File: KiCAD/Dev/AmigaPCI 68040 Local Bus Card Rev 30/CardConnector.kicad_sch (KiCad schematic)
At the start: 42 parts, among them CN100 DIN41612_03x40, CN111 SPI, J100 CPU CLOCK, U111 ICE40HX4K-TQ144, U409F2 W25X20CLSN, X100 40MHz

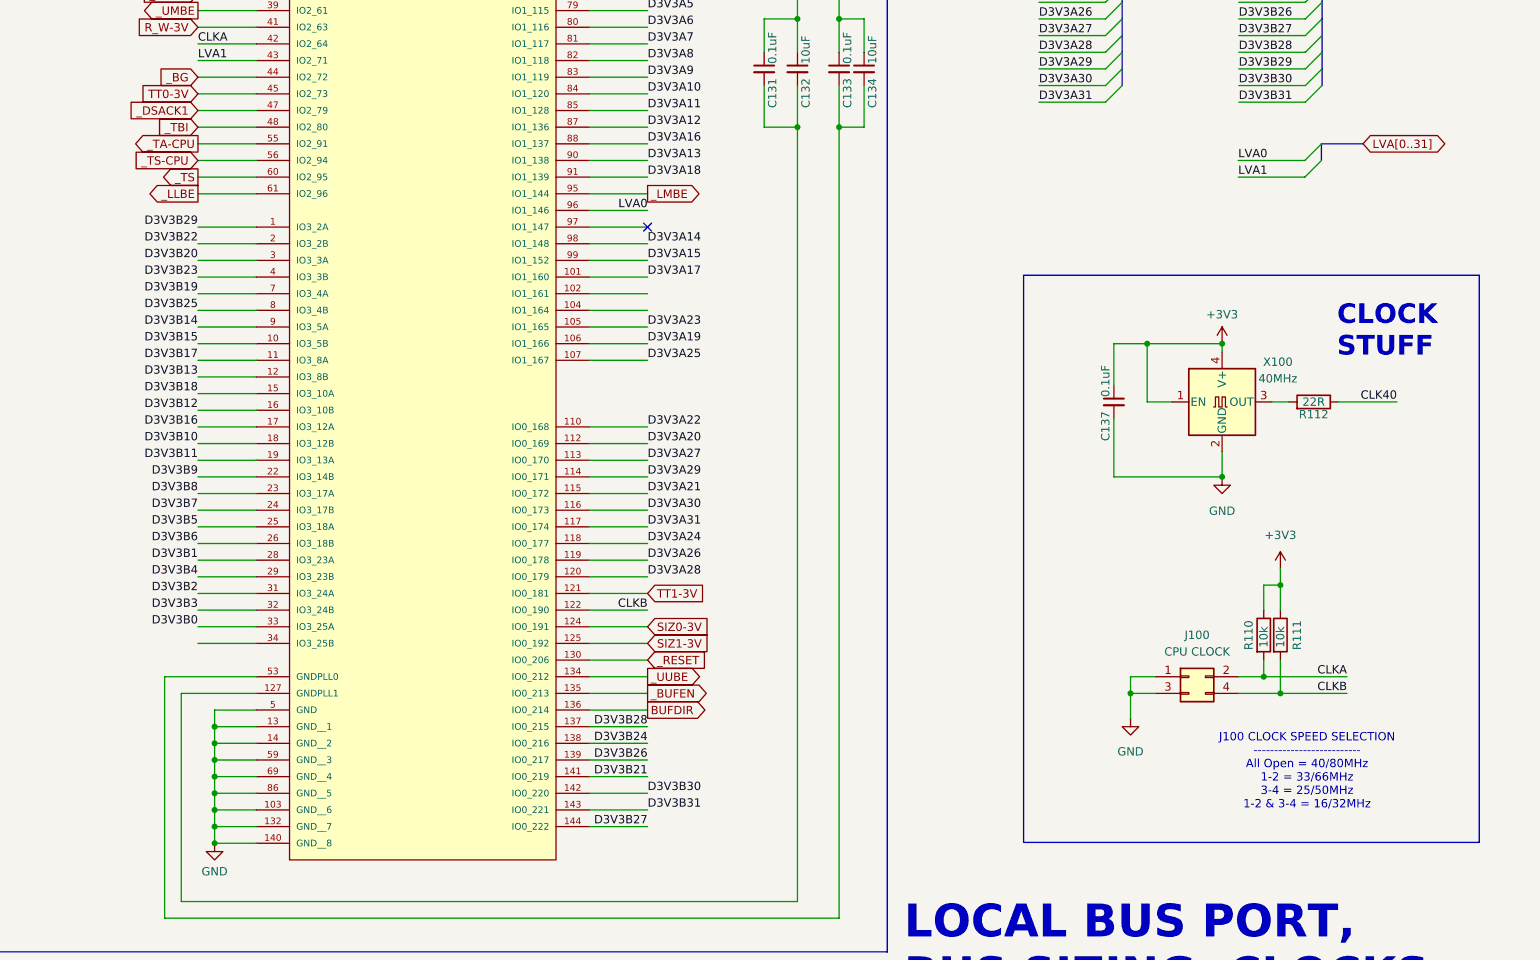
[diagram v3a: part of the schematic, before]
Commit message: CPU Local Bus Card routing. 15-JUL-2024
Board is now 6 layers to provide adequate +5V to the 68040.
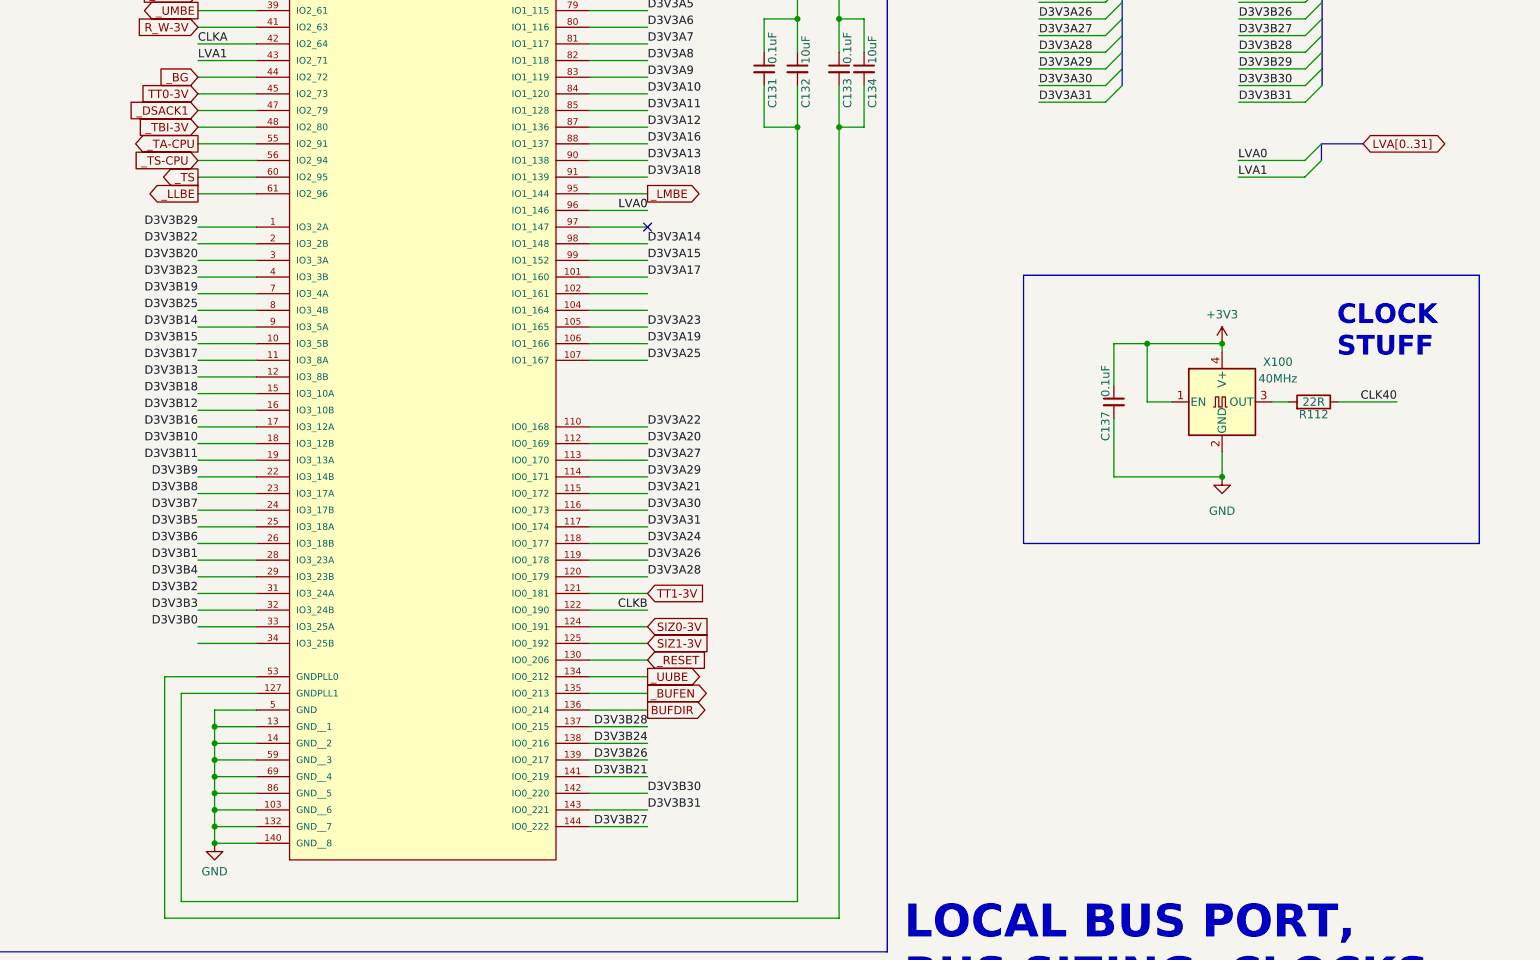
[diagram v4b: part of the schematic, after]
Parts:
- removed J100: CPU CLOCK, Connector_PinHeader_2.54mm:PinHeader_2x02_P2.54mm_Vertical, symbol Connector_Generic:Conn_02x02_Odd_Even
- removed R110, R111: 10k, Resistor_SMD:R_0603_1608Metric, symbol Device:R
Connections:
- net _TBI: no longer U111.48 (IO2_80)
- new net _TBI-3V: U111.48 (IO2_80)
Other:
- note removed: "J100 CLOCK SPEED SELECTION -------------------------- All Open = 40/80MHz 1-2 = 33/66MHz 3-4 = 25/50MHz 1-2 & 3-4 = 16/32MHz"

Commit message: CPU Local Bus Card Rev 3.0 Routing 18-JUL-2024
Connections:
- net CLKB is gone; now on net SIZ0-3V: U111.122 (IO0_190)
- net _TBI-3V is gone; now on net _TBI: U111.48 (IO2_80)
- net LVA0: now also U111.63 (IO2_103_CBSEL0); no longer U111.96 (IO1_146)
- net RAMCLK: now also U111.38 (IO2_57); no longer U111.129 (IO0_198_GBIN0)
- net R_W-3V: now also U111.97 (IO1_147); no longer U111.41 (IO2_63)
- net SIZ0-3V: no longer U111.124 (IO0_191)
- net SIZ1-3V: now also U111.121 (IO0_181); no longer U111.125 (IO0_192)
- net TT1-3V: now also U111.104 (IO1_164); no longer U111.121 (IO0_181)
- net _BG: no longer U111.44 (IO2_72)
- net _DSACK0: now also U111.130 (IO0_206); no longer U111.37 (IO2_56)
- net _RESET: now also U111.34 (IO3_25B); no longer U111.130 (IO0_206)
- net _TA-CPU: now also U111.125 (IO0_192); no longer U111.55 (IO2_91)
- net _TCI: now also U111.41 (IO2_63)
- net _TEA: now also U111.37 (IO2_56)
- net _TS-3V: now also U111.129 (IO0_198_GBIN0); no longer U111.38 (IO2_57)
- net _TBI-CPU: now reaches U111.64 (IO2_104_CBSEL1)
- net _LOCKE renamed _CPURST
- new net _BGA: U111.96 (IO1_146)
- new net _TCI-CPU: U111.44 (IO2_72)
- new net _TEA-CPU: U111.124 (IO0_191)
- no-connect marks 4 -> 2

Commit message: CPU Local Bus Card Rev 3.0 Routing 18-JUL-2024
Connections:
- net _TS-CPU is gone; now on net RAMCLK: U111.56 (IO2_94)
- net +1V2: no longer C135.1
- net +3V3: now also C135.1
- net D3V3A17: now also U111.104 (IO1_164); no longer U111.101 (IO1_160)
- net D3V3A20: now also U111.110 (IO0_168); no longer U111.112 (IO0_169)
- net D3V3A21: now also U111.114 (IO0_171); no longer U111.115 (IO0_172)
- net D3V3A22: now also U111.95 (IO1_144); no longer U111.110 (IO0_168)
- net D3V3A24: now also U111.117 (IO0_174); no longer U111.118 (IO0_177)
- net D3V3A26: now also U111.118 (IO0_177); no longer U111.119 (IO0_178)
- net D3V3A27: now also U111.112 (IO0_169); no longer U111.113 (IO0_170)
- net D3V3A28: now also U111.119 (IO0_178); no longer U111.120 (IO0_179)
- net D3V3A29: now also U111.113 (IO0_170); no longer U111.114 (IO0_171)
- net D3V3A30: now also U111.115 (IO0_172); no longer U111.116 (IO0_173)
- net D3V3A31: now also U111.116 (IO0_173); no longer U111.117 (IO0_174)
- net LVA0: now also U111.38 (IO2_57); no longer U111.63 (IO2_103_CBSEL0)
- net LVA1: now also U111.39 (IO2_61); no longer U111.43 (IO2_71)
- net RAMCLK: no longer U111.38 (IO2_57)
- net SIZ0-3V: now also U111.121 (IO0_181); no longer U111.122 (IO0_190)
- net SIZ1-3V: now also U111.120 (IO0_179); no longer U111.121 (IO0_181)
- net TT0-3V: now also U111.130 (IO0_206); no longer U111.45 (IO2_73)
- net TT1-3V: now also U111.134 (IO0_212); no longer U111.104 (IO1_164)
- net _DSACK0: now also U111.129 (IO0_198_GBIN0); no longer U111.130 (IO0_206)
- net _DSACK1: now also U111.45 (IO2_73); no longer U111.47 (IO2_79)
- net _LBEN: now also U111.47 (IO2_79); no longer U111.62 (IO2_102)
- net _LLBE: now also U111.60 (IO2_95); no longer U111.61 (IO2_96)
- net _LMBE: now also U111.62 (IO2_102); no longer U111.95 (IO1_144)
- net _TA-CPU: now also U111.124 (IO0_191); no longer U111.125 (IO0_192)
- net _TCI: now also U111.43 (IO2_71); no longer U111.41 (IO2_63)
- net _TCI-CPU: now also U111.101 (IO1_160); no longer U111.44 (IO2_72)
- net _TEA-CPU: now also U111.122 (IO0_190); no longer U111.124 (IO0_191)
- net _TS: now also U111.41 (IO2_63); no longer U111.60 (IO2_95)
- net _TS-3V: now also U111.125 (IO0_192); no longer U111.129 (IO0_198_GBIN0)
- net _UMBE: now also U111.63 (IO2_103_CBSEL0); no longer U111.39 (IO2_61)
- net _UUBE: now also U111.61 (IO2_96); no longer U111.134 (IO0_212)
- net CLKA: no longer names the net of U111.42 (IO2_64)
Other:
- moved on the sheet: C117, C135

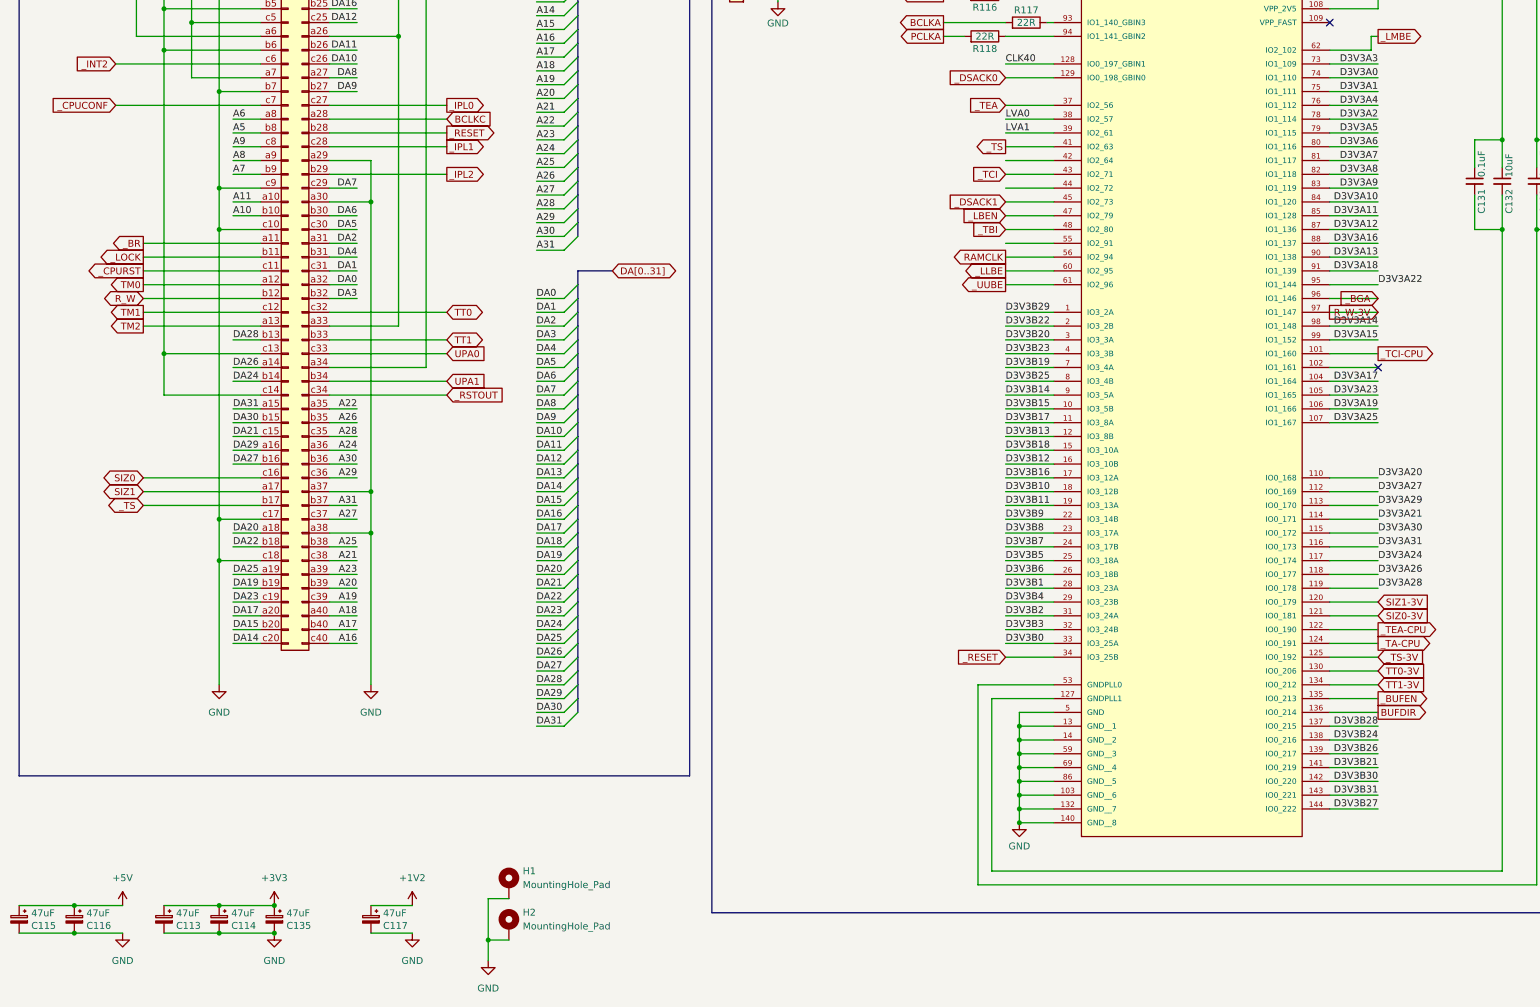
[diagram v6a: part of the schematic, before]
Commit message: CPU Local Bus Card schematics and routing, misc changes to readme's.
This should be project lock for the Rev 3.0 CPU Local Bus Card.
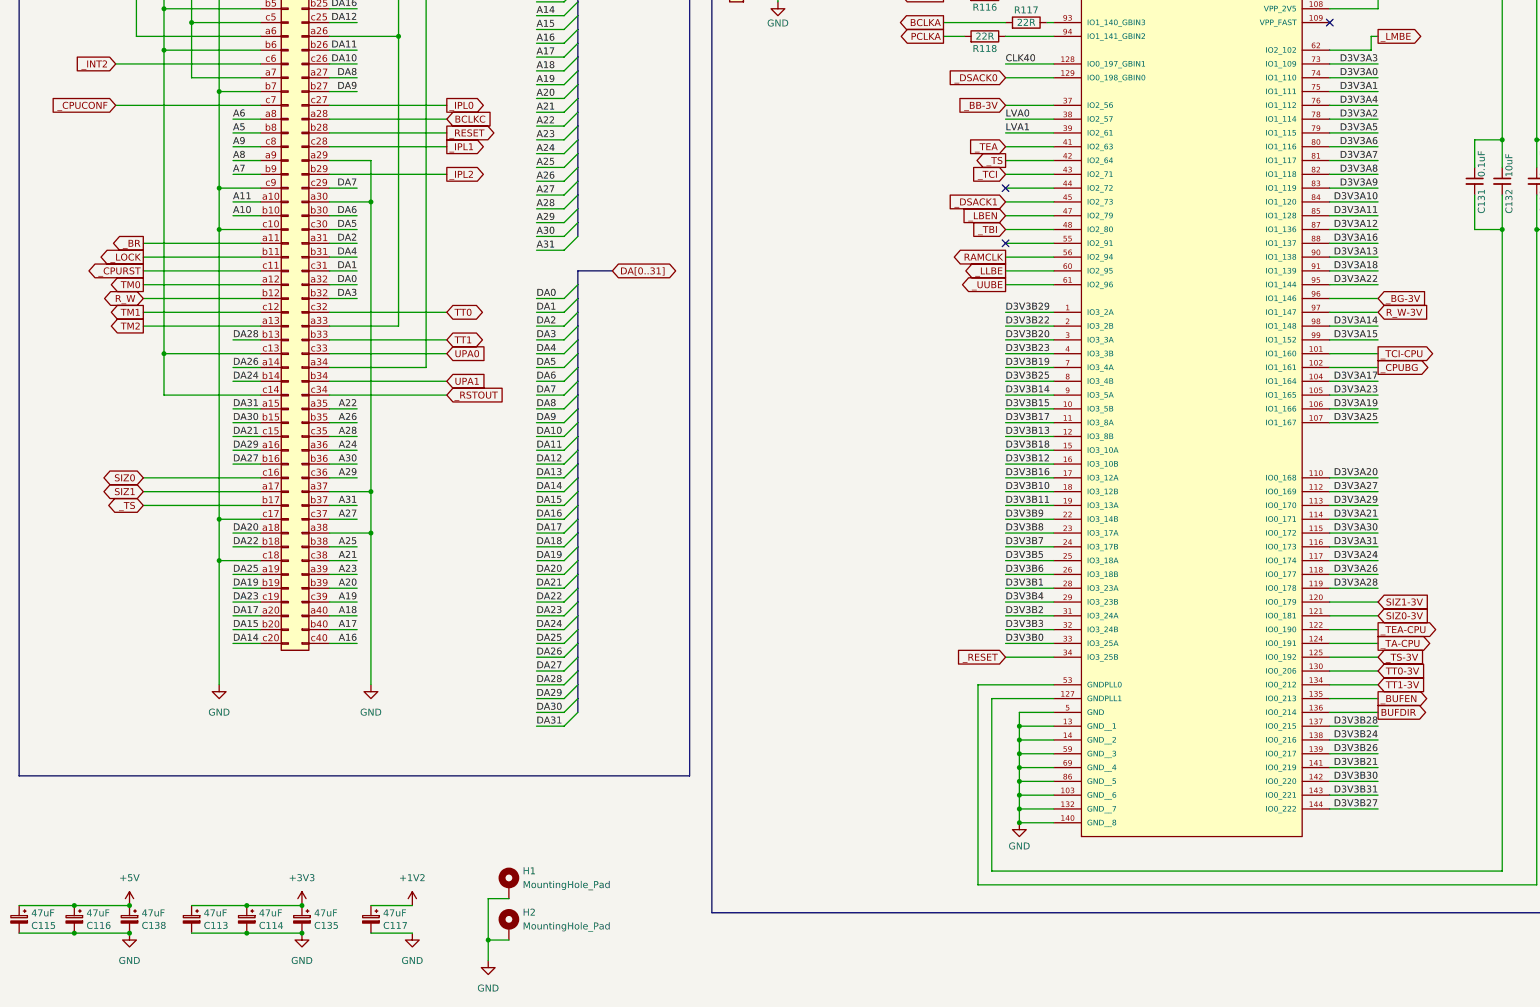
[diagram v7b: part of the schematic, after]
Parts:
- added C138: 47uF, Capacitor_THT:CP_Radial_D5.0mm_P2.00mm, symbol AmigaPCI-Symbols:CP_Small-Device
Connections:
- net +5V: now also C138.1
- net GND: now also C138.2
- net _TEA: now also U111.41 (IO2_63); no longer U111.37 (IO2_56)
- net _TS: now also U111.42 (IO2_64); no longer U111.41 (IO2_63)
- net _CPUBG: now reaches U111.102 (IO1_161)
- net _BGA renamed _BG-3V
- new net _BB-3V: U111.37 (IO2_56)
- no-connect marks 2 -> 3
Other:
- title: AmigaPCI 68040 -> AmigaPCI 68040 Local Bus Card
- moved on the sheet: C113, C114, C135

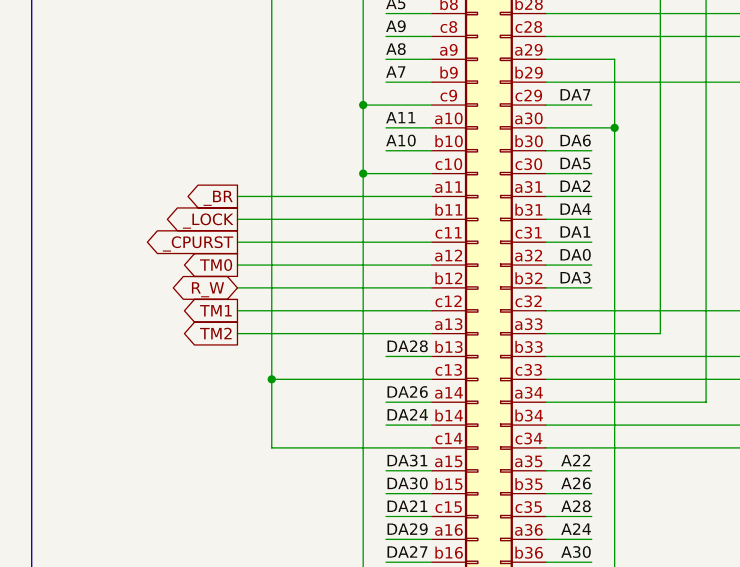
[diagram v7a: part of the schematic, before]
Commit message: Finalize 68040 Local Bus Card.
Added jumper to hold _BG for testing.
Added 22ohm series resistor to R_W.
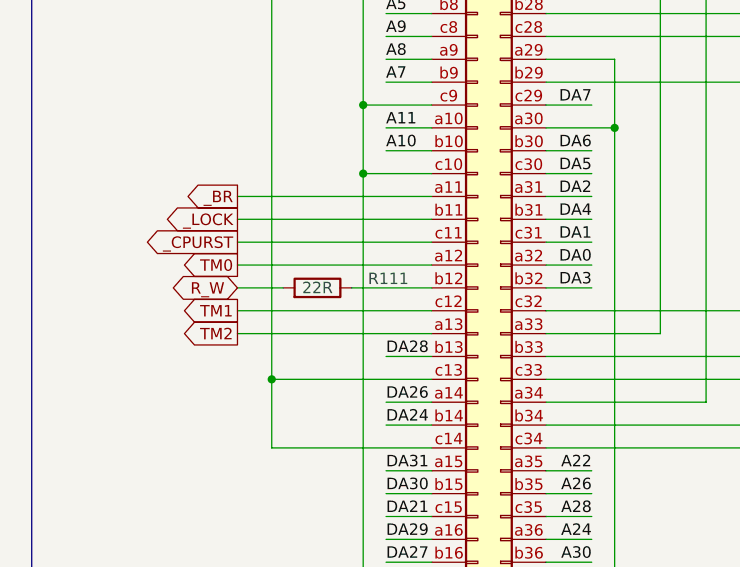
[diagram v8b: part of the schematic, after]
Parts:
- added R111: 22R, Resistor_SMD:R_0603_1608Metric, symbol Device:R
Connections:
- net R_W: now also R111.2; no longer CN100.b12 (Pin_b12)
- new net: CN100.b12 (Pin_b12), R111.1
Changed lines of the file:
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@@
 	(title_block
 		(title "AmigaPCI 68040 Local Bus Card")
-		(date "2024-07-20")
+		(date "2024-07-21")
 		(rev "3.0")
 	)
@@
 	(wire
 		(pts
-			(xy 45.72 130.81) (xy 67.31 130.81)
+			(xy 45.72 130.81) (xy 50.8 130.81)
 		)
 		(stroke
@@
 	(wire
 		(pts
+			(xy 58.42 130.81) (xy 67.31 130.81)
+		)
+		(stroke
+			(width 0)
+			(type default)
+		)
+	)
+	(wire
+		(pts
 			(xy 176.53 48.26) (xy 176.53 50.8)
 		)
@@
 					(unit 1)
 				)
+			)
+		)
+	)
+	(symbol
+		(lib_id "Device:R")
+		(at 54.61 130.81 270)
+		(mirror x)
+		(unit 1)
+		(exclude_from_sim no)
+		(in_bom yes)
+		(on_board yes)
+		(dnp no)
+		(property "Reference" "R111"
+			(at 62.484 129.794 90)
+			(effects
+				(font
+					(size 1.27 1.27)
+				)
+			)
+		)
+		(property "Value" "22R"
+			(at 54.61 130.81 90)
+			(effects
+				(font
+					(size 1.27 1.27)
+				)
+			)
+		)
+		(property "Footprint" "Resistor_SMD:R_0603_1608Metric"
+			(at 54.61 132.588 90)
+			(effects
+				(font
+					(size 1.27 1.27)
+				)
+				(hide yes)
+			)
+		)
+		(property "Datasheet" "~"
+			(at 54.61 130.81 0)
+			(effects
+				(font
+					(size 1.27 1.27)
+				)
+				(hide yes)
+			)
+		)
+		(property "Description" ""
+			(at 54.61 130.81 0)
+			(effects
+				(font
+					(size 1.27 1.27)
+				)
+				(hide yes)
+			)
+		)
+		(pin "1"
+		)
+		(pin "2"
+		)
+		(instances
+			(project "AmigaPCI 68040"
+				(path "/e4eb271a-56d6-4281-ada6-40852f202c68/e434a9c9-dc49-4b97-aed3-c8d4620b07ee"
+					(reference "R111")
+					(unit 1)
+				)
